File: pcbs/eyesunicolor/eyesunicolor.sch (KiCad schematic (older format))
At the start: 21 parts, among them J1 SUPP28, P1 CONN_5X2

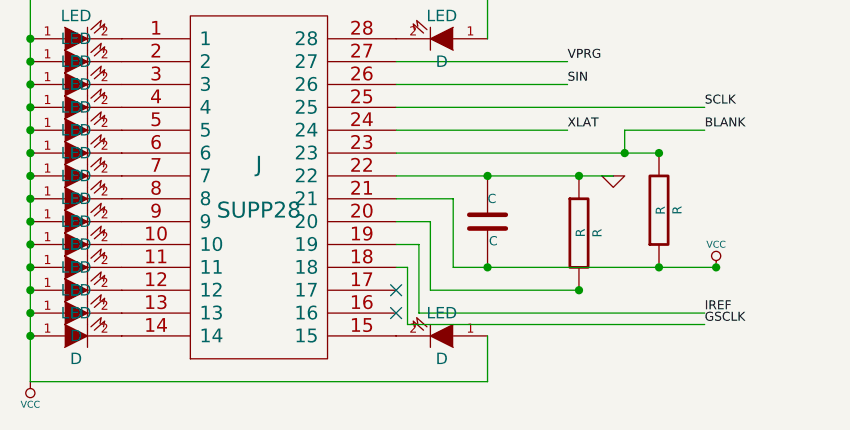
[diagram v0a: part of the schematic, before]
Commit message: Dise?o de placa. Acomodamos los leds.
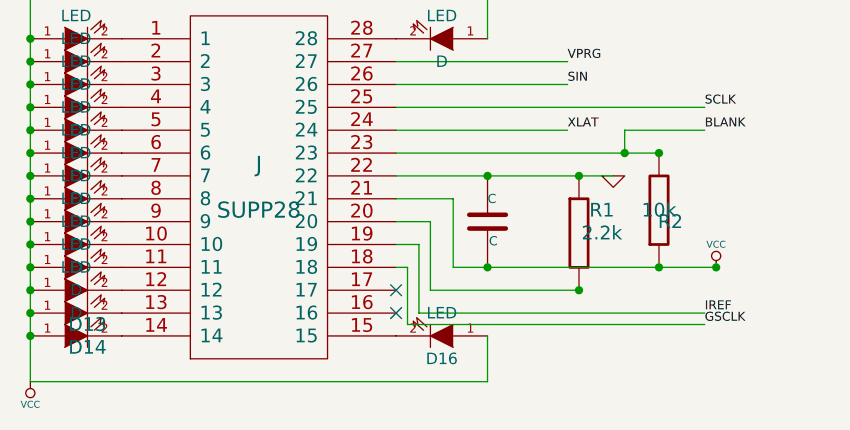
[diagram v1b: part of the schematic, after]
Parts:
- D13, D14: Reference D -> (none); Value LED -> (none)
- D16: footprint (none) -> ~; Reference D -> (none); Value LED -> (none)
- R1: value R -> 2.2k; Reference R -> (none); Value R -> (none)
- R2: value R -> 10k; Reference R -> (none); Value R -> (none)
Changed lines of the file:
@@
-EESchema Schematic File Version 2  date Fri 13 Sep 2013 22:11:05 ART
+EESchema Schematic File Version 2  date Fri 20 Sep 2013 20:11:20 ART
 LIBS:power
 LIBS:device
@@
 Sheet 1 1
 Title ""
-Date "14 sep 2013"
+Date "20 sep 2013"
 Rev ""
 Comp ""
@@
 U 1 1 5233A1A5
 P 5250 3100
-F 0 "D14" H 5300 3150 60  0001 C CNN
+F 0 "D14" H 5300 3150 60  0000 C CNN
 F 1 "LED" H 5250 3100 60  0001 C CNN
 F 2 "" H 5250 3100 60  0001 C CNN
 F 3 "~" H 5250 3100 60  0000 C CNN
-F 4 "D" H 5250 3200 50  0000 C CNN "Reference"
-F 5 "LED" H 5250 3000 50  0000 C CNN "Value"
-F 6 "~" H 5250 3100 60  0000 C CNN "Footprint"
 	1    5250 3100
 	1    0    0    1
@@
 U 1 1 5233A218
 P 5250 3000
-F 0 "D13" H 5300 3050 60  0001 C CNN
+F 0 "D13" H 5300 3050 60  0000 C CNN
 F 1 "LED" H 5250 3000 60  0001 C CNN
 F 2 "" H 5250 3000 60  0001 C CNN
 F 3 "~" H 5250 3000 60  0000 C CNN
-F 4 "D" H 5250 3100 50  0000 C CNN "Reference"
-F 5 "LED" H 5250 2900 50  0000 C CNN "Value"
-F 6 "~" H 5250 3000 60  0000 C CNN "Footprint"
 	1    5250 3000
 	1    0    0    1
@@
 	1    5250 1800
 	1    0    0    1
-$EndComp
-$Comp
-L LED D16
-U 1 1 5233A28D
-P 6850 3100
-F 0 "D16" H 6900 3150 60  0001 C CNN
-F 1 "LED" H 6850 3100 60  0001 C CNN
-F 2 "" H 6850 3100 60  0001 C CNN
-F 3 "~" H 6850 3100 60  0000 C CNN
-F 4 "D" H 6850 3200 50  0000 C CNN "Reference"
-F 5 "LED" H 6850 3000 50  0000 C CNN "Value"
-F 6 "~" H 6850 3100 60  0000 C CNN "Footprint"
-	1    6850 3100
-	-1   0    0    1
 $EndComp
 $Comp
@@
 $EndComp
 $Comp
-L VCC #PWR01
+L VCC #PWR1
 U 1 1 5233A481
 P 5050 3300
-F 0 "#PWR01" H 5100 3350 60  0001 C CNN
+F 0 "#PWR1" H 5100 3350 60  0001 C CNN
 F 1 "VCC" H 5050 3300 60  0001 C CNN
 F 2 "" H 5050 3300 60  0001 C CNN
@@
 U 1 1 5233A555
 P 7800 2550
-F 0 "R2" H 7850 2600 60  0001 C CNN
-F 1 "R" H 7800 2550 60  0001 C CNN
+F 0 "R2" H 7850 2600 60  0000 C CNN
+F 1 "10k" H 7800 2550 60  0000 C CNN
 F 2 "" H 7800 2550 60  0001 C CNN
 F 3 "~" H 7800 2550 30  0000 C CNN
-F 4 "R" V 7880 2550 40  0000 C CNN "Reference"
-F 5 "R" V 7807 2551 40  0000 C CNN "Value"
-F 6 "~" V 7730 2550 30  0000 C CNN "Footprint"
 	1    7800 2550
 	1    0    0    1
@@
 U 1 1 5233A6CE
 P 7450 2650
-F 0 "R1" H 7500 2700 60  0001 C CNN
-F 1 "R" H 7450 2650 60  0001 C CNN
+F 0 "R1" H 7550 2750 60  0000 C CNN
+F 1 "2.2k" H 7550 2650 60  0000 C CNN
 F 2 "" H 7450 2650 60  0001 C CNN
 F 3 "~" H 7450 2650 30  0000 C CNN
-F 4 "R" V 7530 2650 40  0000 C CNN "Reference"
-F 5 "R" V 7457 2651 40  0000 C CNN "Value"
-F 6 "~" V 7380 2650 30  0000 C CNN "Footprint"
 	1    7450 2650
 	1    0    0    -1
@@
 $EndComp
 $Comp
-L VCC #PWR02
+L VCC #PWR3
 U 1 1 5233A73F
 P 8050 2800
-F 0 "#PWR02" H 8100 2850 60  0001 C CNN
+F 0 "#PWR3" H 8100 2850 60  0001 C CNN
 F 1 "VCC" H 8050 2800 60  0001 C CNN
 F 2 "" H 8050 2800 60  0001 C CNN
@@
 $EndComp
 $Comp
-L GND #PWR?
+L GND #PWR5
 U 1 1 5233B383
 P 9950 2700
-AR Path="/5233B400" Ref="#PWR?"  Part="1"
-AR Path="/5233B383" Ref="#PWR03"  Part="1"
-F 0 "#PWR03" H 10000 2750 60  0001 C CNN
+F 0 "#PWR5" H 10000 2750 60  0001 C CNN
 F 1 "GND" H 9950 2700 60  0001 C CNN
 F 2 "" H 9950 2700 60  0001 C CNN
@@
 	9650 2550 9950 2550
 $Comp
-L VCC #PWR04
+L VCC #PWR4
 U 1 1 5233B56F
 P 9950 2550
-F 0 "#PWR04" H 10000 2600 60  0001 C CNN
+F 0 "#PWR4" H 10000 2600 60  0001 C CNN
 F 1 "VCC" H 9950 2550 60  0001 C CNN
 F 2 "" H 9950 2550 60  0001 C CNN
@@
 Connection ~ 9650 2650
 $Comp
-L GND #PWR05
+L GND #PWR2
 U 1 1 5233B64A
 P 7600 2400
-F 0 "#PWR05" H 7650 2450 60  0001 C CNN
+F 0 "#PWR2" H 7650 2450 60  0001 C CNN
 F 1 "GND" H 7600 2400 60  0001 C CNN
 F 2 "" H 7600 2400 60  0001 C CNN
@@
 	1    0    0    -1
 $EndComp
+$Comp
+L LED D16
+U 1 1 523CD500
+P 6850 3100
+F 0 "D16" H 6850 3200 50  0000 C CNN
+F 1 "LED" H 6850 3000 50  0000 C CNN
+F 2 "~" H 6850 3100 60  0000 C CNN
+F 3 "~" H 6850 3100 60  0000 C CNN
+	1    6850 3100
+	-1   0    0    1
+$EndComp
 $EndSCHEMATC

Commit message: Termine la placa. Hay que optimizarla.
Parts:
- D1, D15, D4, D6, D7: Reference D -> (none); Value LED -> (none)
- D10: renamed from D9; Reference D -> (none); Value LED -> (none)
- D11: renamed from D2; Reference D -> (none); Value LED -> (none)
- D13: renamed from D11; Reference D -> (none); Value LED -> (none)
- D16: renamed from D3; Reference D -> (none); Value LED -> (none)
- D2: renamed from D12; Reference D -> (none); Value LED -> (none)
- D5: renamed from D8; Reference D -> (none); Value LED -> (none)
- D8: renamed from D5; Reference D -> (none); Value LED -> (none)
- D9: renamed from D10; Reference D -> (none); Value LED -> (none)
- renumbered D13 to D12, D16 to D3
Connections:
- net GND: now also P1.10; no longer P1.8
- net GSCLK: now also P1.2; no longer P1.4
- net IREF: now also P1.6; no longer P1.2
- net VCC: now also P1.8; no longer P1.6
- net at J1.1: now also D7.2 (K); no longer D1.2 (K)
- net at J1.10: now also D15.2 (K); no longer D9.2 (K)
- net at J1.14: now also D11.2 (K); no longer D14.2 (K)
- net at J1.15: now also D1.2 (K); no longer D3.2 (K)
- net at J1.2: now also D8.2 (K); no longer D11.2 (K)
- net at J1.28: now also D6.2 (K); no longer D15.2 (K)
- net at J1.3: now also D5.2 (K); no longer D16.2 (K)
- net at J1.5: now also D9.2 (K); no longer D8.2 (K)
- net at J1.6: now also D10.2 (K); no longer D6.2 (K)
- net at J1.7: now also D14.2 (K); no longer D7.2 (K)
- net at J1.8: now also D3.2 (K); no longer D5.2 (K)
- net at J1.9: now also D16.2 (K); no longer D10.2 (K)
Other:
- moved on the sheet: D14, D3

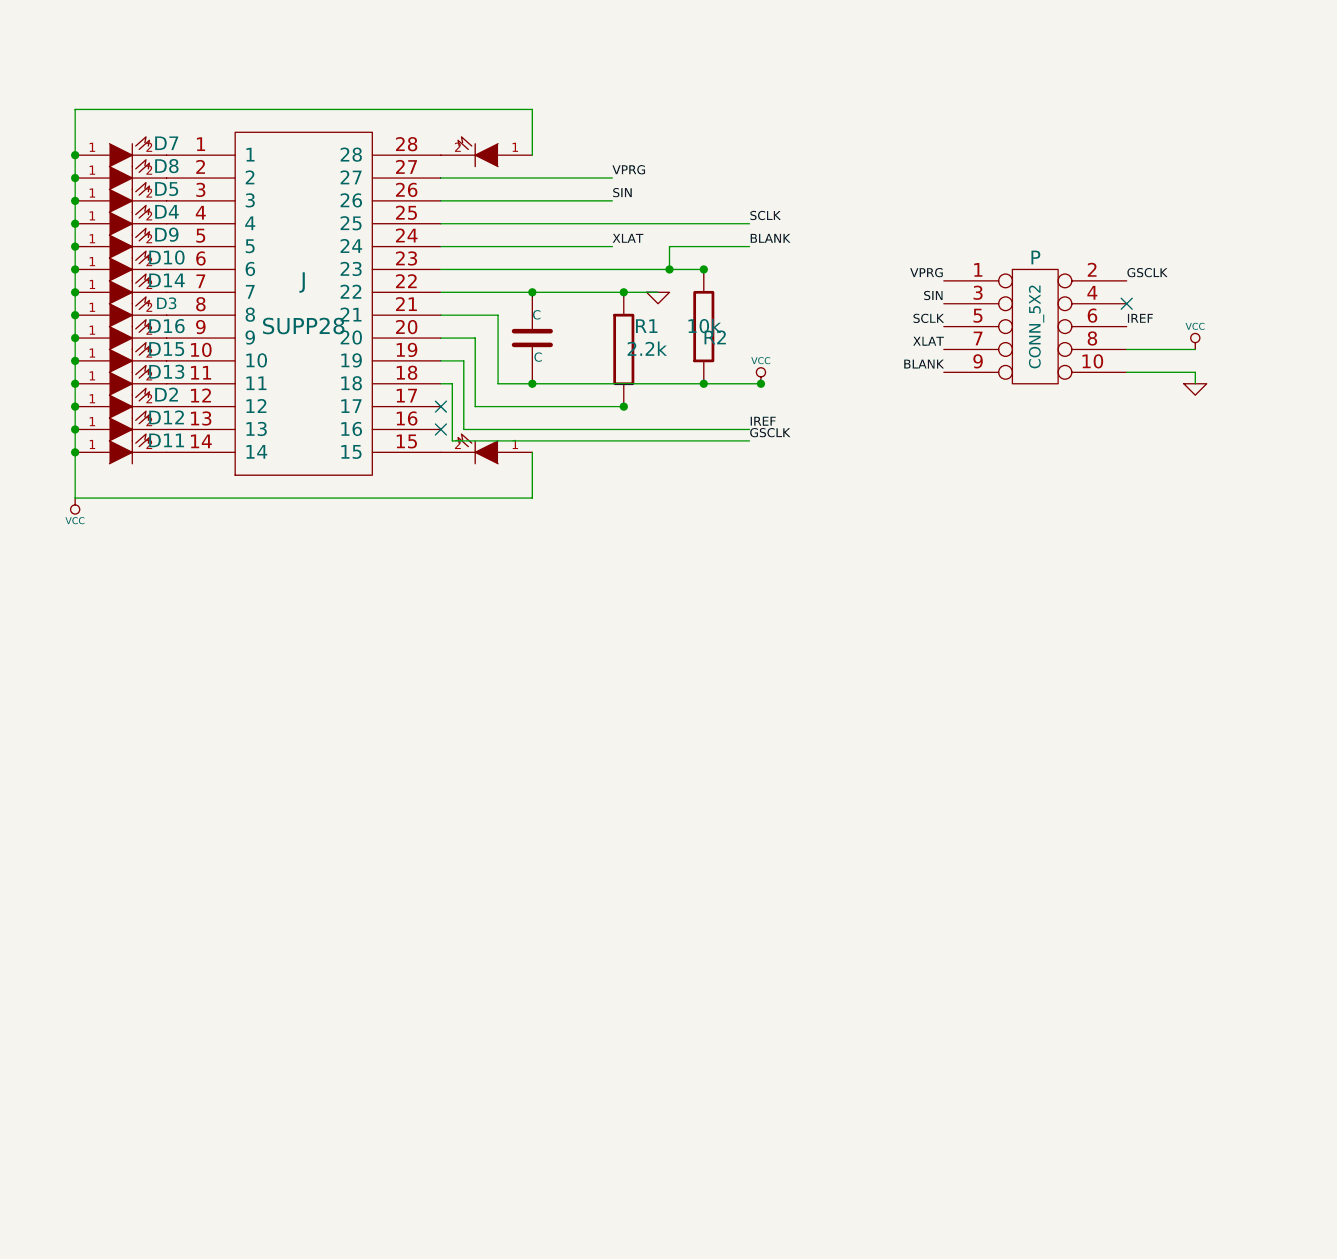
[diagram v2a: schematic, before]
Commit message: Se termino el PCB del ojo izquierdo, se comenzo a trabajar con el ojo derecho
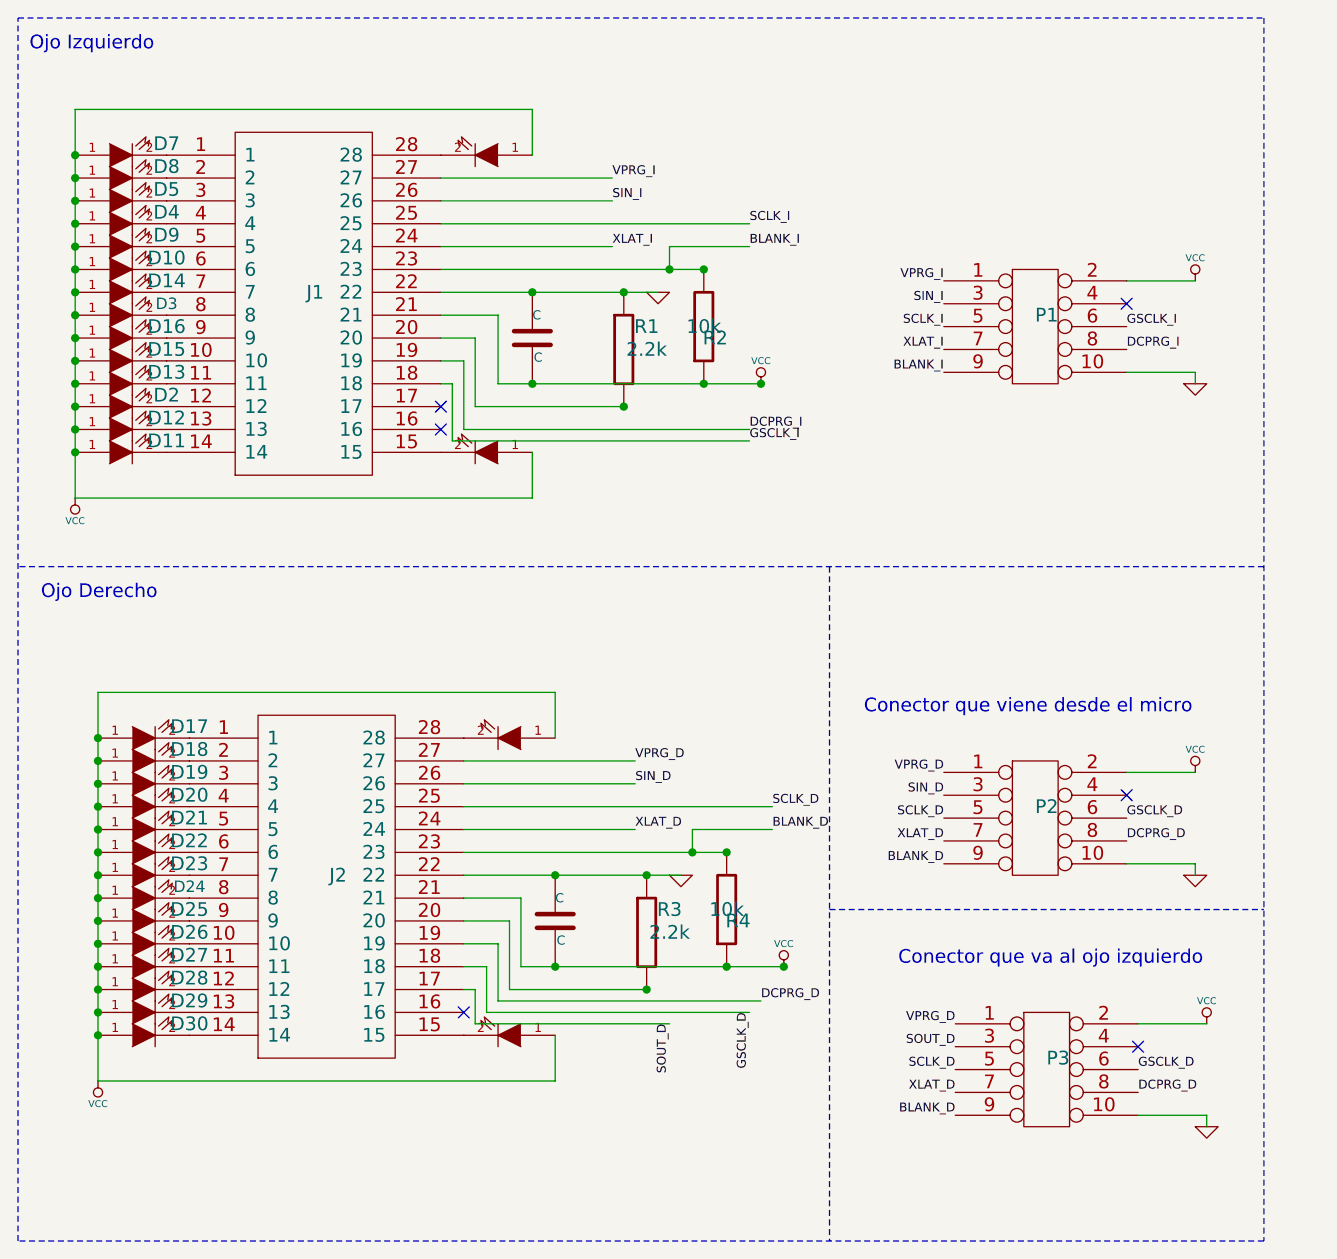
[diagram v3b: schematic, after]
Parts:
- added C2: C, symbol C
- added D17, D18, D19, D20, D21, D22, D23, D25, D26, D27, D28, D29, D30, D31, D32: LED, symbol LED
- added D24: LED, ~, symbol LED
- added J2: SUPP28, symbol SUPP28
- added P2, P3: CONN_5X2, symbol CONN_5X2
- added R3: 2.2k, symbol R
- added R4: 10k, symbol R
- J1: Reference J -> (none); Value SUPP28 -> (none)
- P1: Reference P -> (none); Value CONN_5X2 -> (none)
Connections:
- net GND: now also C2.1, J2.22, P2.10, P3.10, R3.1
- net VCC: now also P1.2, C2.2, D17.1 (A), D18.1 (A), D19.1 (A), D20.1 (A), D21.1 (A), D22.1 (A), D23.1 (A), D24.1 (A), D25.1 (A), D26.1 (A), D27.1 (A), D28.1 (A), D29.1 (A), D30.1 (A), D31.1 (A), D32.1 (A), J2.21, P2.2, P3.2, R4.1; no longer P1.8
- net BLANK renamed BLANK_I
- net GSCLK renamed GSCLK_I
- net GSCLK_I: now also P1.6; no longer P1.2
- net IREF renamed DCPRG_I
- net DCPRG_I: now also P1.8; no longer P1.6
- net SCLK renamed SCLK_I
- net SIN renamed SIN_I
- net VPRG renamed VPRG_I
- net XLAT renamed XLAT_I
- new net: D17.2 (K), J2.1
- new net: D26.2 (K), J2.10
- new net: D27.2 (K), J2.11
- new net: D28.2 (K), J2.12
- new net: D29.2 (K), J2.13
- new net: D30.2 (K), J2.14
- new net: D32.2 (K), J2.15
- new net: D18.2 (K), J2.2
- new net: J2.20, R3.2
- new net: D31.2 (K), J2.28
- new net: D19.2 (K), J2.3
- new net: D20.2 (K), J2.4
- new net: D21.2 (K), J2.5
- new net: D22.2 (K), J2.6
- new net: D23.2 (K), J2.7
- new net: D24.2 (K), J2.8
- new net: D25.2 (K), J2.9
- new net BLANK_D: J2.23, P2.9, P3.9, R4.2
- new net DCPRG_D: J2.19, P2.8, P3.8
- new net GSCLK_D: J2.18, P2.6, P3.6
- new net SCLK_D: J2.25, P2.5, P3.5
- new net SIN_D: J2.26, P2.3
- new net SOUT_D: J2.17, P3.3
- new net VPRG_D: J2.27, P2.1, P3.1
- new net XLAT_D: J2.24, P2.7, P3.7
- no-connect marks 3 -> 6
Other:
- note added: "Conector que va al ojo izquierdo"
- note added: "Conector que viene desde el micro"
- note added: "Ojo Derecho"
- note added: "Ojo Izquierdo"

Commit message: Arme el pcb del ojo derecho. Falta termiar
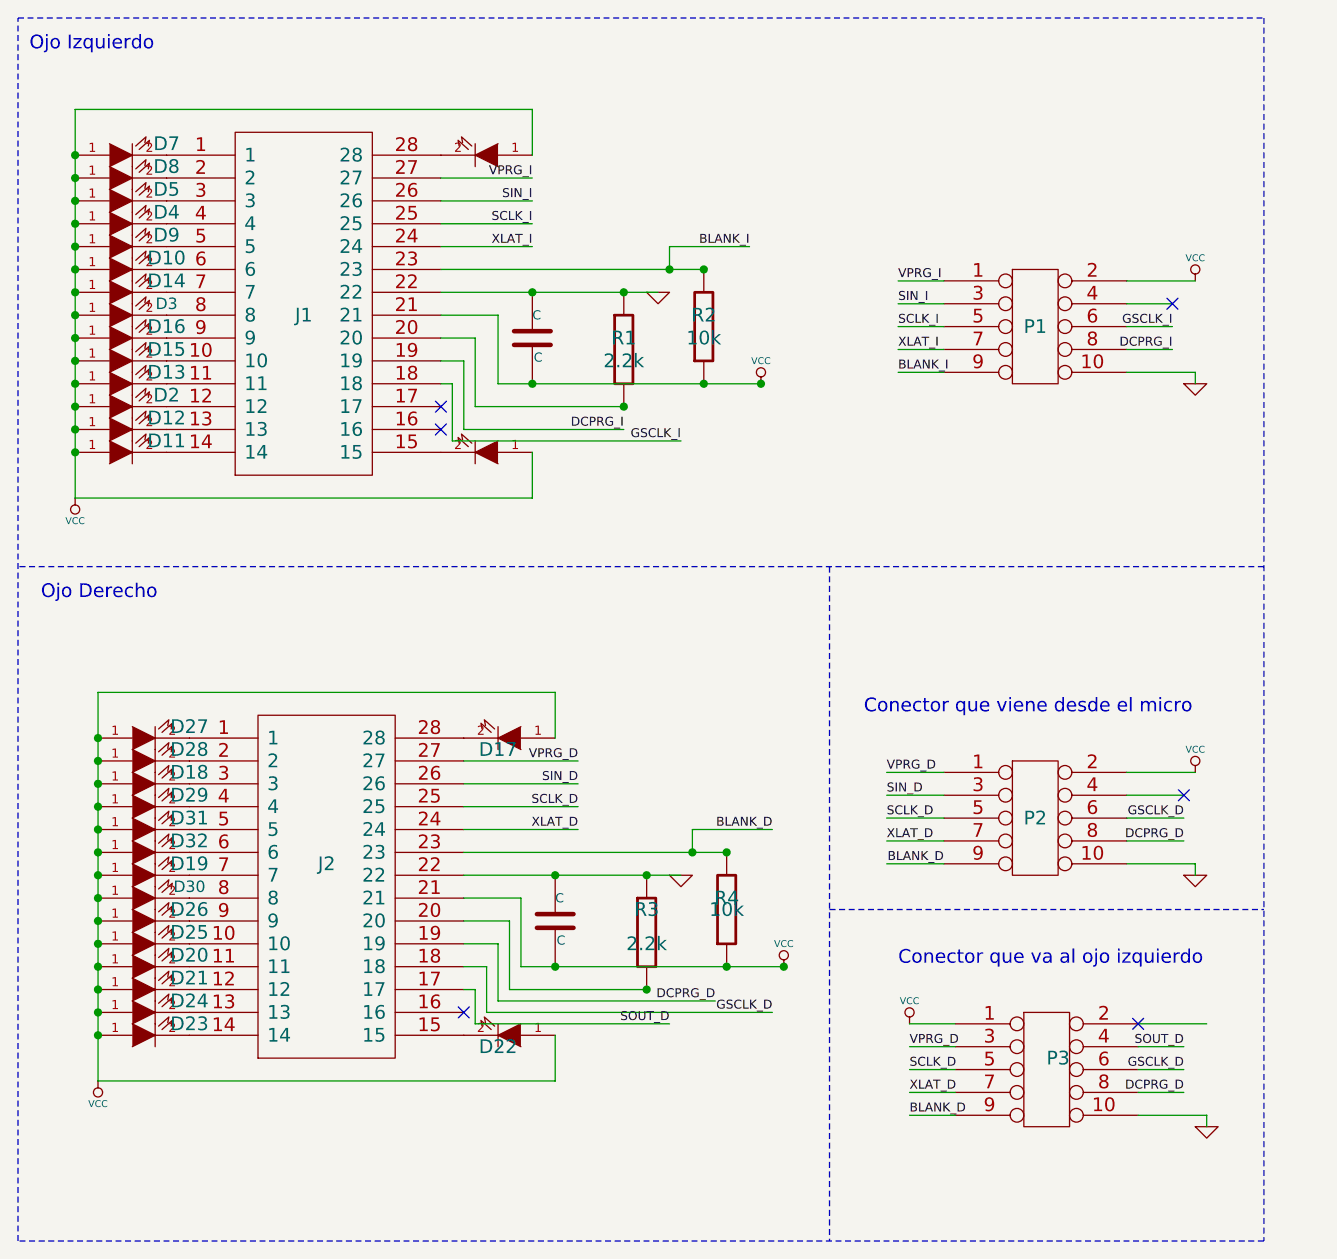
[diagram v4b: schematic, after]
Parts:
- renumbered D31 to D17, D19 to D18, D23 to D19, D27 to D20, D28 to D21, D32 to D22, D30 to D23, D29 to D24, D26 to D25, D25 to D26, D17 to D27, D18 to D28, D20 to D29, D24 to D30, D21 to D31, D22 to D32
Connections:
- net SOUT_D: now also P3.4; no longer P3.3
- net VCC: now also P3.1; no longer P3.2
- net VPRG_D: now also P3.3; no longer P3.1
